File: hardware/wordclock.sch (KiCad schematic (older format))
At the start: 15 parts, among them K1 CONN_3, P1 ISP, P2 CONN_2, U1 ATmega168, U2 DS1307, U3 7805, U4 4094, U5 4017, X1 32.768kHz

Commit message: Beginning of PCB layout.
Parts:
- BT1: footprint (none) -> CR2032H
- C1, C4, C5: footprint (none) -> C1
- C2, C3: footprint (none) -> C1V7
- K1: value CONN_3 -> SERIAL; footprint (none) -> PIN_ARRAY_3X1
- P1: footprint (none) -> pin_array_3x2
- P2: value CONN_2 -> Vin; footprint (none) -> SIL-2
- U1: footprint DIL28 -> DIP-28__300
- U2: footprint MODULE -> DIP-8__300
- U3: footprint (none) -> TO220
- U4, U5: footprint (none) -> DIP-16__300
- X1: footprint (none) -> r26-crystal
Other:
- note added: "ADD PULL UPS ON I2C!!!"
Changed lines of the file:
@@
-EESchema Schematic File Version 2  date Thu 10 May 2012 01:29:50 BST
+EESchema Schematic File Version 2  date Tue 19 Jun 2012 03:11:31 BST
 LIBS:power
 LIBS:device
@@
 Sheet 1 2
 Title "Wordclock"
-Date "10 may 2012"
+Date "19 jun 2012"
 Rev "1"
 Comp "David Robertson"
@@
 Comment4 ""
 $EndDescr
+Text Notes 3200 1250 0    60   ~ 0
+ADD PULL UPS ON I2C!!!
 Connection ~ 2200 4100
 Connection ~ 2200 4100
@@
 F 0 "C1" H 2250 3050 50  0000 L CNN
 F 1 "0.1uF" H 2250 2850 50  0000 L CNN
+F 2 "C1" H 2200 2950 60  0001 C CNN
 	1    2200 2950
 	1    0    0    -1
@@
 F 0 "C4" H 6250 2100 50  0000 L CNN
 F 1 "0.1uF" V 6000 2000 50  0000 L CNN
+F 2 "C1" H 6200 2000 60  0001 C CNN
 	1    6200 2000
 	1    0    0    -1
@@
 F 0 "C5" H 6250 3400 50  0000 L CNN
 F 1 "0.1uF" V 6000 3300 50  0000 L CNN
+F 2 "C1" H 6200 3300 60  0001 C CNN
 	1    6200 3300
 	1    0    0    -1
@@
 F 0 "C3" H 5650 7150 50  0000 L CNN
 F 1 "47uF" H 5650 6950 50  0000 L CNN
+F 2 "C1V7" H 5600 7050 60  0001 C CNN
 	1    5600 7050
 	1    0    0    -1
@@
 F 0 "C2" H 4550 7150 50  0000 L CNN
 F 1 "1uF" H 4550 6950 50  0000 L CNN
+F 2 "C1V7" H 4500 7050 60  0001 C CNN
 	1    4500 7050
 	1    0    0    -1
@@
 P 3800 7350
 F 0 "P2" V 3750 7350 40  0000 C CNN
-F 1 "CONN_2" V 3850 7350 40  0000 C CNN
+F 1 "Vin" V 3850 7350 40  0000 C CNN
+F 2 "SIL-2" H 3800 7350 60  0001 C CNN
 	1    3800 7350
 	-1   0    0    1
@@
 F 0 "U3" H 5200 6604 60  0000 C CNN
 F 1 "7805" H 5050 7000 60  0000 C CNN
+F 2 "TO220" H 5050 6800 60  0001 C CNN
 	1    5050 6800
 	1    0    0    -1
@@
 P 3900 2350
 F 0 "K1" V 3850 2350 50  0000 C CNN
-F 1 "CONN_3" V 3950 2350 40  0000 C CNN
+F 1 "SERIAL" V 3950 2350 40  0000 C CNN
+F 2 "PIN_ARRAY_3X1" H 3900 2350 60  0001 C CNN
 	1    3900 2350
 	1    0    0    -1
@@
 F 0 "BT1" H 1050 7400 50  0000 C CNN
 F 1 "BATTERY" H 1050 7010 50  0000 C CNN
+F 2 "CR2032H" H 1050 7200 60  0001 C CNN
 	1    1050 7200
 	1    0    0    -1
@@
 F 0 "P1" H 3700 4550 50  0000 C CNN
 F 1 "ISP" V 3700 4350 40  0000 C CNN
+F 2 "pin_array_3x2" H 3700 4300 60  0001 C CNN
 	1    3700 4300
 	1    0    0    -1
@@
 F 0 "U4" H 6050 2300 50  0000 C CNN
 F 1 "4094" H 5850 2300 50  0000 C CNN
+F 2 "DIP-16__300" H 6150 1850 60  0001 C CNN
 	1    6150 1850
 	1    0    0    -1
@@
 F 0 "U5" H 5900 2900 60  0000 C CNN
 F 1 "4017" H 5950 2800 60  0000 C CNN
+F 2 "DIP-16__300" H 6150 3350 60  0001 C CNN
 	1    6150 3350
 	1    0    0    -1
@@
 F 0 "X1" H 1050 6700 60  0000 C CNN
 F 1 "32.768kHz" H 1050 6400 60  0000 C CNN
+F 2 "r26-crystal" H 1050 6550 60  0001 C CNN
 	1    1050 6550
 	1    0    0    -1
@@
 F 0 "U2" H 2300 6600 50  0000 C CNN
 F 1 "DS1307" H 2300 6800 50  0000 C CNN
-F 2 "MODULE" H 2300 6700 50  0001 C CNN
+F 2 "DIP-8__300" H 2300 6700 50  0001 C CNN
 F 3 "DOCUMENTATION" H 2300 6700 50  0001 C CNN
 	1    2300 6700
@@
 F 0 "U1" H 1500 3850 50  0000 L BNN
 F 1 "ATmega168" H 2450 1200 50  0000 L BNN
-F 2 "DIL28" H 2700 1125 50  0001 C CNN
+F 2 "DIP-28__300" H 2700 1125 50  0001 C CNN
 	1    2200 2600
 	1    0    0    -1

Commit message: REV. A PCB nearly complete.
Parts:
- added R1, R2: 4k7, symbol R
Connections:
- net +5V: now also R1.1, R2.1
- net SCL: now also R1.2
- net SDA: now also R2.2
- net Vin: now reaches C2.1, P2.2 (PM), U3.1 (VI)

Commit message: Mostly done PCB.
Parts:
- added P5: Vin-alt, SIL-2, symbol CONN_2
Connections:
- net GND: now also P5.1 (P1)
- net Vin: now also P5.2 (PM)
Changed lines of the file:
@@
-EESchema Schematic File Version 2  date Tue 19 Jun 2012 06:52:00 BST
+EESchema Schematic File Version 2  date Wed 20 Jun 2012 20:38:20 BST
 LIBS:power
 LIBS:device
@@
 Sheet 1 2
 Title "Wordclock"
-Date "19 jun 2012"
+Date "20 jun 2012"
 Rev "1"
 Comp "David Robertson"
@@
 Comment4 ""
 $EndDescr
+Connection ~ 4250 7450
+Wire Wire Line
+	4250 7450 4250 7600
+Wire Wire Line
+	4250 7600 3500 7600
+Wire Wire Line
+	3500 7600 3500 7000
+Wire Wire Line
+	3500 7000 4000 7000
+Wire Wire Line
+	4000 7000 4000 6700
 Connection ~ 3100 6550
 Wire Wire Line
@@
 	4500 7250 4500 7450
 Wire Wire Line
-	4650 6750 4150 6750
-Wire Wire Line
-	4150 6750 4150 7250
+	4150 6750 4650 6750
 Wire Wire Line
 	3550 2450 3550 2550
@@
 	2200 7450 2250 7450
 Connection ~ 2250 7450
+Wire Wire Line
+	4150 7250 4150 6500
+Wire Wire Line
+	4150 6500 4000 6500
+Connection ~ 4150 6750
+$Comp
+L CONN_2 P5
+U 1 1 4FE2267B
+P 3650 6600
+F 0 "P5" V 3600 6600 40  0000 C CNN
+F 1 "Vin-alt" V 3700 6600 40  0000 C CNN
+F 2 "SIL-2" H 3650 6600 60  0001 C CNN
+	1    3650 6600
+	-1   0    0    1
+$EndComp
 Text Label 4300 6750 0    60   ~ 0
 Vin

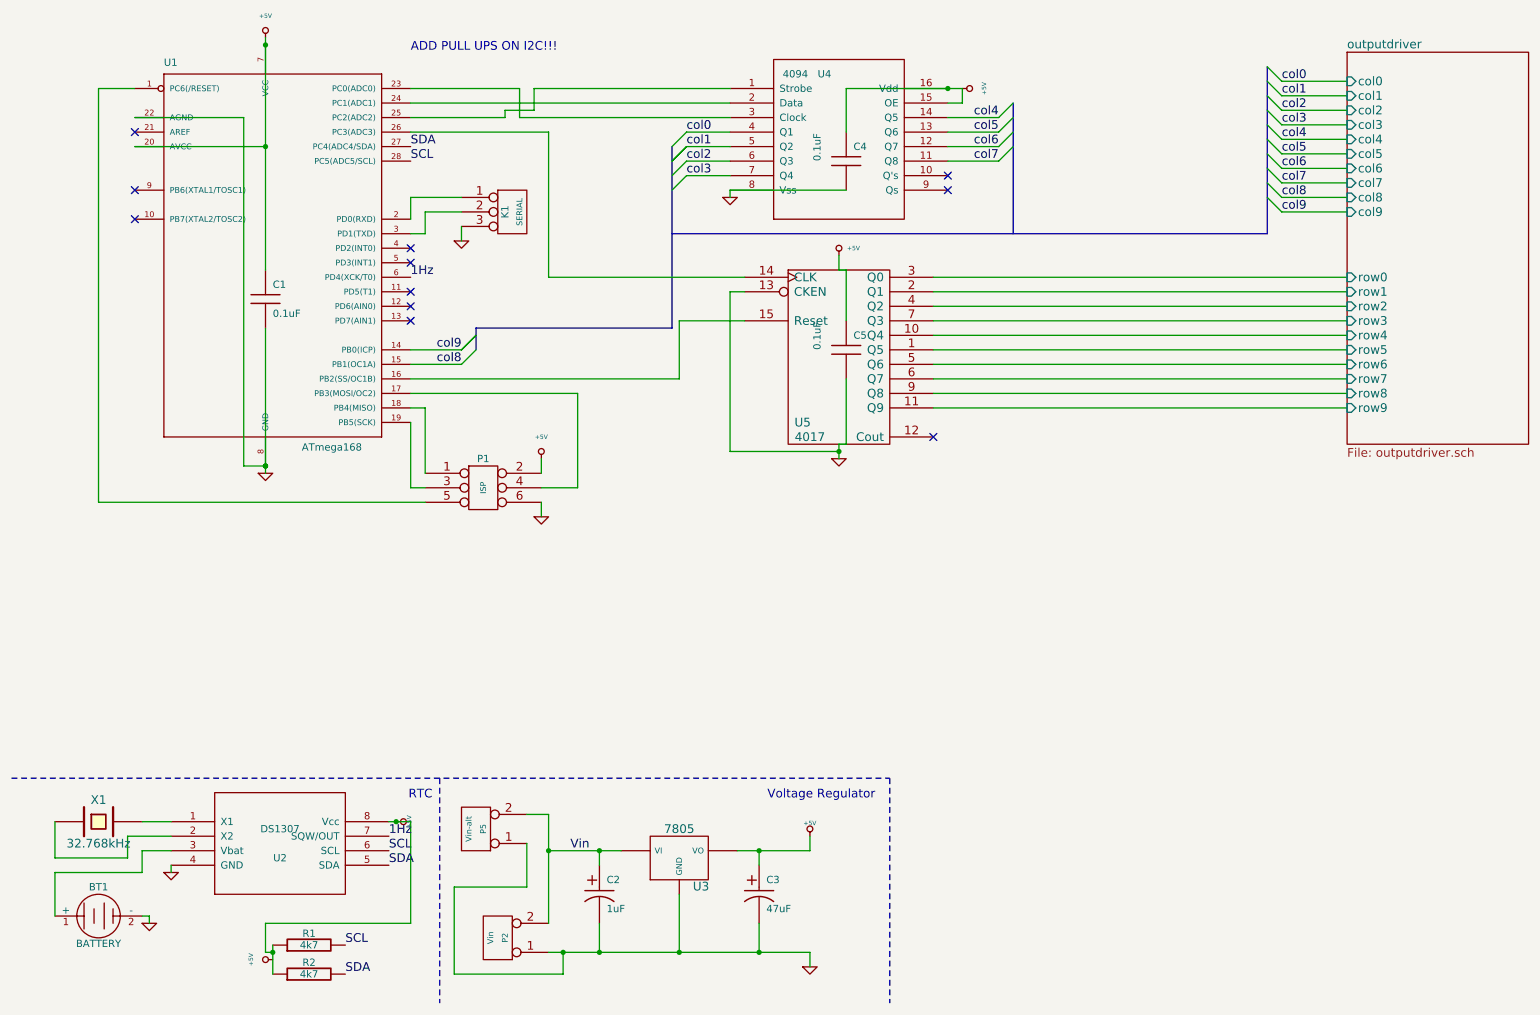
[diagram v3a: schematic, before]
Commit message: Added time set buttons to schematic.
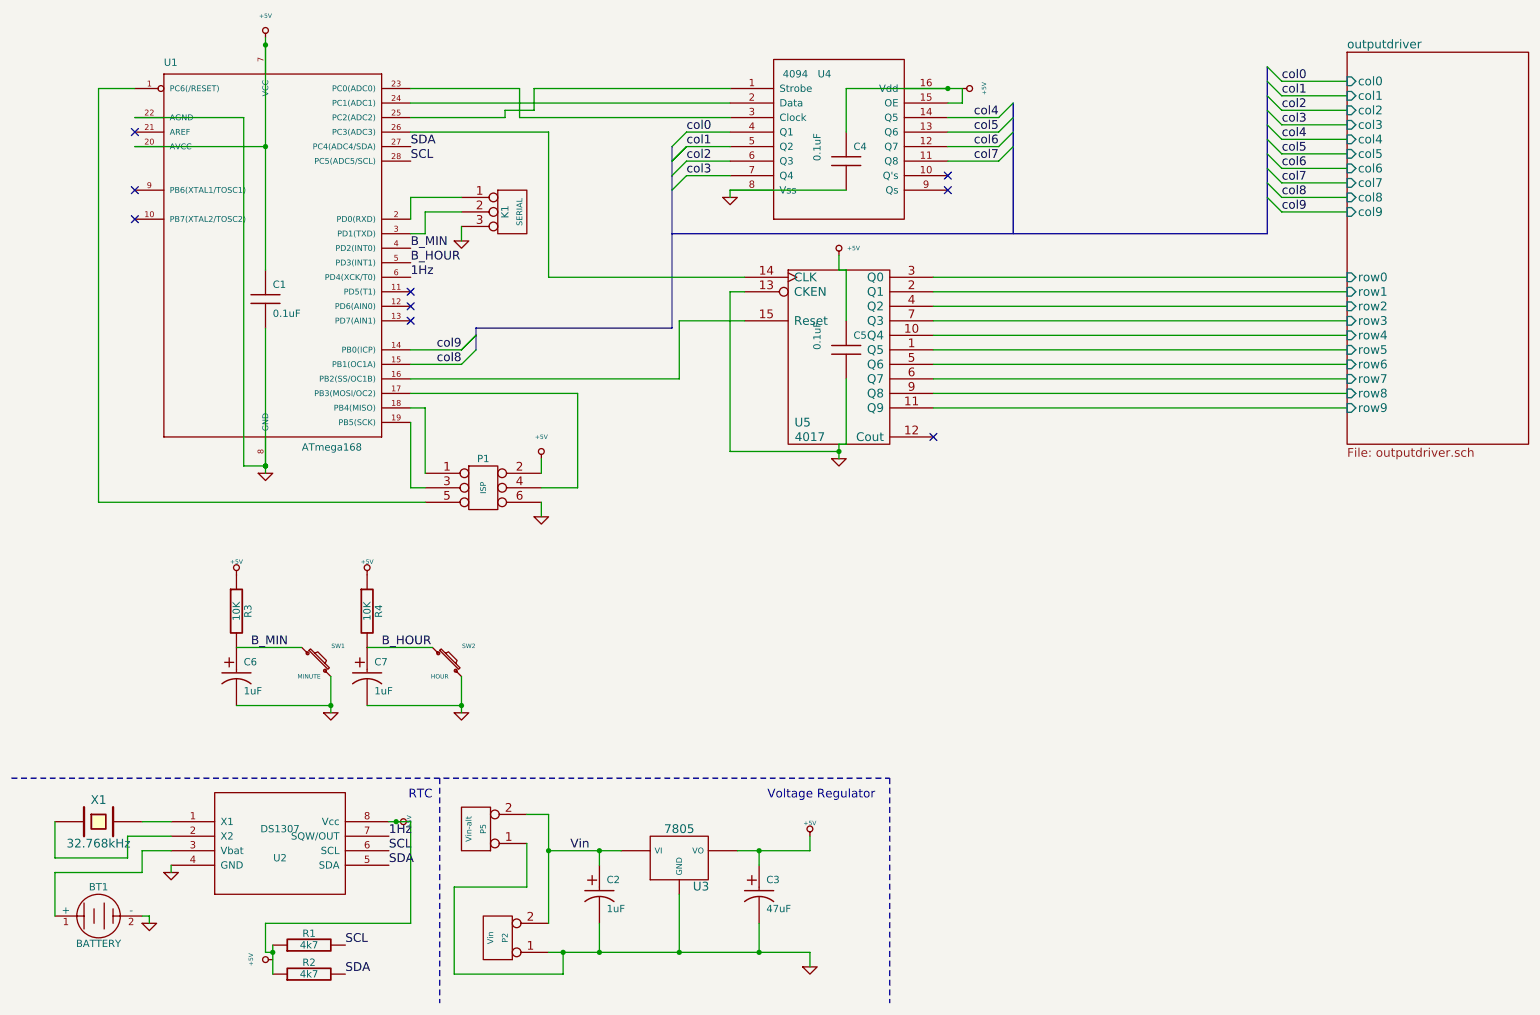
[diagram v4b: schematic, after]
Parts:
- added C6, C7: 1uF, symbol CP1
- added R3, R4: 10K, symbol R
- added SW1: MINUTE, symbol SW_PUSH_SMALL
- added SW2: HOUR, symbol SW_PUSH_SMALL
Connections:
- net +5V: now also R3.1, R4.1
- net GND: now also C6.2, C7.2, SW1.2, SW2.2
- net B_MIN: now reaches U1.4 (PD2(INT0))
- net B_MIN: now also C6.1, R3.2, SW1.1
- net B_HOUR: now reaches U1.5 (PD3(INT1))
- net B_HOUR: now also C7.1, R4.2, SW2.1
- no-connect marks 11 -> 9
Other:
- note removed: "ADD PULL UPS ON I2C!!!"
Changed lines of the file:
@@
-EESchema Schematic File Version 2  date Wed 20 Jun 2012 20:38:20 BST
+EESchema Schematic File Version 2  date Wed 11 Jul 2012 22:54:35 BST
 LIBS:power
 LIBS:device
@@
 Sheet 1 2
 Title "Wordclock"
-Date "20 jun 2012"
+Date "11 jul 2012"
 Rev "1"
 Comp "David Robertson"
@@
 Comment4 ""
 $EndDescr
+$Comp
+L SW_PUSH_SMALL SW2
+U 1 1 4FFDF2DD
+P 3450 5450
+F 0 "SW2" H 3600 5560 30  0000 C CNN
+F 1 "HOUR" H 3400 5350 30  0000 C CNN
+	1    3450 5450
+	1    0    0    -1
+$EndComp
+$Comp
+L CP1 C7
+U 1 1 4FFDF2DC
+P 2900 5550
+F 0 "C7" H 2950 5650 50  0000 L CNN
+F 1 "1uF" H 2950 5450 50  0000 L CNN
+	1    2900 5550
+	1    0    0    -1
+$EndComp
+Text Label 3000 5350 0    60   ~ 0
+B_HOUR
+$Comp
+L R R4
+U 1 1 4FFDF2DB
+P 2900 5100
+F 0 "R4" V 2980 5100 50  0000 C CNN
+F 1 "10K" V 2900 5100 50  0000 C CNN
+	1    2900 5100
+	1    0    0    -1
+$EndComp
+$Comp
+L GND #PWR01
+U 1 1 4FFDF2DA
+P 3550 5800
+F 0 "#PWR01" H 3550 5800 30  0001 C CNN
+F 1 "GND" H 3550 5730 30  0001 C CNN
+	1    3550 5800
+	1    0    0    -1
+$EndComp
+Wire Wire Line
+	3550 5800 3550 5550
+Wire Wire Line
+	2900 5350 3350 5350
+Wire Wire Line
+	2900 5750 3550 5750
+Connection ~ 3550 5750
+$Comp
+L +5V #PWR02
+U 1 1 4FFDF2D9
+P 2900 4850
+F 0 "#PWR02" H 2900 4940 20  0001 C CNN
+F 1 "+5V" H 2900 4940 30  0000 C CNN
+	1    2900 4850
+	1    0    0    -1
+$EndComp
+$Comp
+L +5V #PWR03
+U 1 1 4FFDF2C9
+P 2000 4850
+F 0 "#PWR03" H 2000 4940 20  0001 C CNN
+F 1 "+5V" H 2000 4940 30  0000 C CNN
+	1    2000 4850
+	1    0    0    -1
+$EndComp
+Connection ~ 2650 5750
+Wire Wire Line
+	2000 5750 2650 5750
+Wire Wire Line
+	2000 5350 2450 5350
 Connection ~ 4250 7450
 Wire Wire Line
@@
 	3050 6550 3200 6550
 Wire Wire Line
-	2250 7600 2250 7400
+	2250 7400 2250 7600
 Connection ~ 2200 1900
 Wire Wire Line
-	2200 2750 2200 1150
+	2200 1150 2200 2750
 Wire Wire Line
 	6200 2200 5400 2200
@@
 	5950 6750 5450 6750
 Wire Wire Line
-	5600 6750 5600 6850
+	5600 6850 5600 6750
 Connection ~ 4500 7450
 Wire Wire Line
 	4500 7250 4500 7450
 Wire Wire Line
-	4150 6750 4650 6750
+	4650 6750 4150 6750
 Wire Wire Line
 	3550 2450 3550 2550
@@
 	750  6900 750  7200
 Wire Bus Line
-	7350 2500 7350 1600
+	7350 1600 7350 2500
 Wire Wire Line
 	5400 1800 5100 1800
@@
 Connection ~ 6900 1500
 Wire Wire Line
-	2200 3150 2200 4150
+	2200 4150 2200 3150
 Connection ~ 2200 4100
 Connection ~ 2200 4100
@@
 	4150 6500 4000 6500
 Connection ~ 4150 6750
+Wire Wire Line
+	2650 5800 2650 5550
+$Comp
+L GND #PWR04
+U 1 1 4FFDF297
+P 2650 5800
+F 0 "#PWR04" H 2650 5800 30  0001 C CNN
+F 1 "GND" H 2650 5730 30  0001 C CNN
+	1    2650 5800
+	1    0    0    -1
+$EndComp
+$Comp
+L R R3
+U 1 1 4FFDF27A
+P 2000 5100
+F 0 "R3" V 2080 5100 50  0000 C CNN
+F 1 "10K" V 2000 5100 50  0000 C CNN
+	1    2000 5100
+	1    0    0    -1
+$EndComp
+Text Label 3200 2700 0    60   ~ 0
+B_HOUR
+Text Label 3200 2600 0    60   ~ 0
+B_MIN
+Text Label 2100 5350 0    60   ~ 0
+B_MIN
+$Comp
+L CP1 C?
+U 1 1 4FFDF1A6
+P 2000 5550
+AR Path="/4FFDF19E" Ref="C?"  Part="1"
+AR Path="/4FFDF1A6" Ref="C6"  Part="1"
+F 0 "C6" H 2050 5650 50  0000 L CNN
+F 1 "1uF" H 2050 5450 50  0000 L CNN
+	1    2000 5550
+	1    0    0    -1
+$EndComp
+$Comp
+L SW_PUSH_SMALL SW?
+U 1 1 4FFDF13E
+P 2550 5450
+AR Path="/4FFDF125" Ref="SW?"  Part="1"
+AR Path="/4FFDF13E" Ref="SW1"  Part="1"
+F 0 "SW1" H 2700 5560 30  0000 C CNN
+F 1 "MINUTE" H 2500 5350 30  0000 C CNN
+	1    2550 5450
+	1    0    0    -1
+$EndComp
 $Comp
 L CONN_2 P5
@@
 Vin
 $Comp
-L +5V #PWR01
+L +5V #PWR05
 U 1 1 4FDFF8A7
 P 2250 7500
-F 0 "#PWR01" H 2250 7590 20  0001 C CNN
+F 0 "#PWR05" H 2250 7590 20  0001 C CNN
 F 1 "+5V" H 2250 7650 30  0000 C CNN
 	1    2250 7500
@@
 	0    -1   -1   0
 $EndComp
-Text Notes 3200 1250 0    60   ~ 0
-ADD PULL UPS ON I2C!!!
 $Comp
 L C C1
@@
 Voltage Regulator
 $Comp
-L GND #PWR02
+L GND #PWR06
 U 1 1 4FAB0608
 P 1400 7250
-F 0 "#PWR02" H 1400 7250 30  0001 C CNN
+F 0 "#PWR06" H 1400 7250 30  0001 C CNN
 F 1 "GND" H 1400 7180 30  0001 C CNN
 	1    1400 7250
@@
 $EndComp
 $Comp
-L +5V #PWR03
+L +5V #PWR07
 U 1 1 4FAB05EC
 P 5950 6650
-F 0 "#PWR03" H 5950 6740 20  0001 C CNN
+F 0 "#PWR07" H 5950 6740 20  0001 C CNN
 F 1 "+5V" H 5950 6740 30  0000 C CNN
 	1    5950 6650
@@
 $EndComp
 $Comp
-L GND #PWR04
+L GND #PWR08
 U 1 1 4FAB05E1
 P 5950 7550
-F 0 "#PWR04" H 5950 7550 30  0001 C CNN
+F 0 "#PWR08" H 5950 7550 30  0001 C CNN
 F 1 "GND" H 5950 7480 30  0001 C CNN
 	1    5950 7550
@@
 $EndComp
 $Comp
-L GND #PWR05
+L GND #PWR09
 U 1 1 4FAB056E
 P 3550 2550
-F 0 "#PWR05" H 3550 2550 30  0001 C CNN
+F 0 "#PWR09" H 3550 2550 30  0001 C CNN
 F 1 "GND" H 3550 2480 30  0001 C CNN
 	1    3550 2550
@@
 NoConn ~ 3200 3000
 NoConn ~ 3200 2900
-NoConn ~ 3200 2600
-NoConn ~ 3200 2700
 Text Notes 3350 6400 2    60   ~ 0
 RTC
@@
 $EndComp
 $Comp
-L +5V #PWR06
+L +5V #PWR010
 U 1 1 4FAAF7B7
 P 4100 4050
-F 0 "#PWR06" H 4100 4140 20  0001 C CNN
+F 0 "#PWR010" H 4100 4140 20  0001 C CNN
 F 1 "+5V" H 4100 4200 30  0000 C CNN
 	1    4100 4050
@@
 NoConn ~ 1300 2400
 $Comp
-L GND #PWR07
+L GND #PWR011
 U 1 1 4FAAF757
 P 4100 4450
-F 0 "#PWR07" H 4100 4450 30  0001 C CNN
+F 0 "#PWR011" H 4100 4450 30  0001 C CNN
 F 1 "GND" H 4100 4380 30  0001 C CNN
 	1    4100 4450
@@
 NoConn ~ 6900 2100
 $Comp
-L +5V #PWR08
+L +5V #PWR012
 U 1 1 4FAAF0EA
 P 7000 1500
-F 0 "#PWR08" H 7000 1590 20  0001 C CNN
+F 0 "#PWR012" H 7000 1590 20  0001 C CNN
 F 1 "+5V" H 7000 1650 30  0000 C CNN
 	1    7000 1500
@@
 $EndComp
 $Comp
-L GND #PWR09
+L GND #PWR013
 U 1 1 4FAAF091
 P 5400 2250
-F 0 "#PWR09" H 5400 2250 30  0001 C CNN
+F 0 "#PWR013" H 5400 2250 30  0001 C CNN
 F 1 "GND" H 5400 2180 30  0001 C CNN
 	1    5400 2250
@@
 1Hz
 $Comp
-L +5V #PWR010
+L +5V #PWR014
 U 1 1 4FAAEF1A
 P 3100 6550
-F 0 "#PWR010" H 3100 6640 20  0001 C CNN
+F 0 "#PWR014" H 3100 6640 20  0001 C CNN
 F 1 "+5V" H 3100 6640 30  0000 C CNN
 	1    3100 6550
@@
 $EndComp
 $Comp
-L +5V #PWR011
+L +5V #PWR015
 U 1 1 4FAAEF0F
 P 2200 1150
-F 0 "#PWR011" H 2200 1240 20  0001 C CNN
+F 0 "#PWR015" H 2200 1240 20  0001 C CNN
 F 1 "+5V" H 2200 1300 30  0000 C CNN
 	1    2200 1150
@@
 $EndComp
 $Comp
-L +5V #PWR012
+L +5V #PWR016
 U 1 1 4FAAEF01
 P 6150 2650
-F 0 "#PWR012" H 6150 2740 20  0001 C CNN
+F 0 "#PWR016" H 6150 2740 20  0001 C CNN
 F 1 "+5V" H 6250 2700 30  0000 C CNN
 	1    6150 2650
@@
 $EndComp
 $Comp
-L GND #PWR013
+L GND #PWR017
 U 1 1 4FAAEED9
 P 6150 4050
-F 0 "#PWR013" H 6150 4050 30  0001 C CNN
+F 0 "#PWR017" H 6150 4050 30  0001 C CNN
 F 1 "GND" H 6150 3980 30  0001 C CNN
 	1    6150 4050
@@
 $EndComp
 $Comp
-L GND #PWR014
+L GND #PWR018
 U 1 1 4FAAEEA0
 P 2200 4150
-F 0 "#PWR014" H 2200 4150 30  0001 C CNN
+F 0 "#PWR018" H 2200 4150 30  0001 C CNN
 F 1 "GND" H 2200 4080 30  0001 C CNN
 	1    2200 4150
@@
 $EndComp
 $Comp
-L GND #PWR015
+L GND #PWR019
 U 1 1 4FAAEE8C
 P 1550 6900
-F 0 "#PWR015" H 1550 6900 30  0001 C CNN
+F 0 "#PWR019" H 1550 6900 30  0001 C CNN
 F 1 "GND" H 1550 6830 30  0001 C CNN
 	1    1550 6900
